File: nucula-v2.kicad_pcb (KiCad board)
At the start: 4 copper layers, 60 x 110 mm, 130 parts, among them J1 USB4105-GF-A-120, J2 JST-PH / 1S Li-ion, J3 KEYBOARD / USER FIT, J4 MAIN LINK / OPTIONAL, J5 MODULE LINK / OPTIONAL, Q1 IRLML6402, Q2 BSS138, Q3 IRLML6402, Q4 BSS138, Q5 BSS138, SW1 RESET, SW2 BOOT, U1 TP4054-42-SOT25R, U2 SY8089AAAC, U3 ESP32-C3-WROOM-02-N4, U4 USBLC6-2SC6, U5 TLV803EA30DBZR, U6 PN7160A1HN/C100E, U7 AP3012KTR-E1, U8 PCF8574T, U9 MCP1700T-3002E/TT, Y1 27.12MHz / CL 10pF

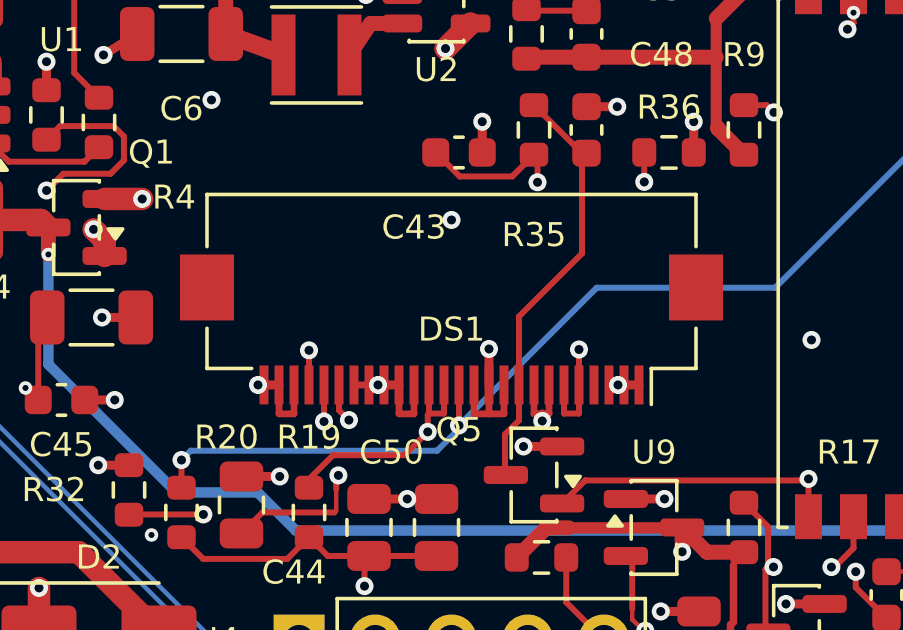
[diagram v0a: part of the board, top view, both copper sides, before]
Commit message: Correct OLED interface and routing for 24-pin display
Replace the 26-contact OLED symbol and socket with the verified CON24 pinout and Hirose FH12-24S connector. Preserve DS1 placement and all other board geometry while rerouting its local pad escapes. Update purchasing data, design exports and regression checks.

Validation: zero ERC/DRC errors, no unconnected items or schematic parity issues; 54 layout/regression checks pass; all 261 scoped simulation results unchanged. The two existing U3 silkscreen-edge warnings remain.
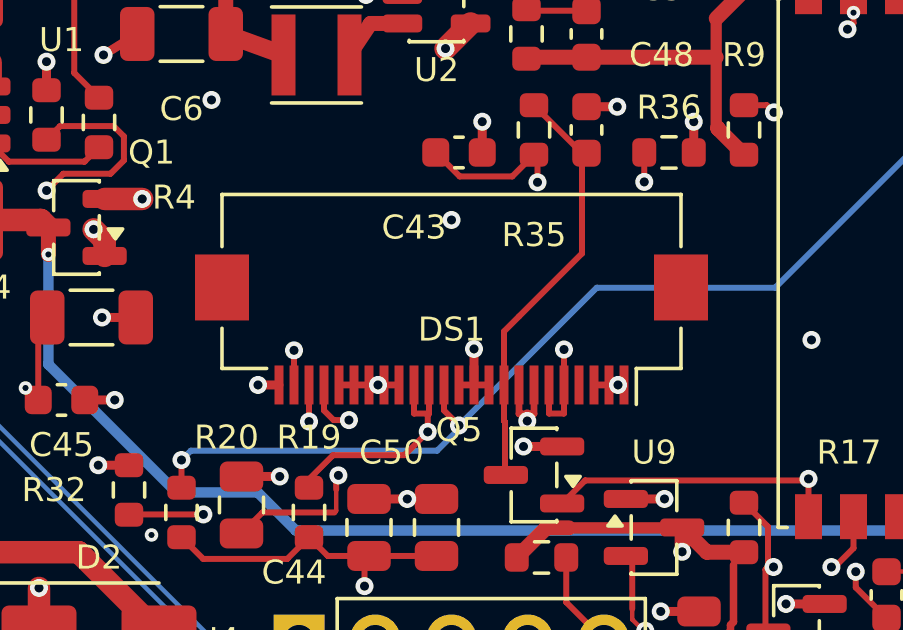
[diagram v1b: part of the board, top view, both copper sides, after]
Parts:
- DS1: value SSD1309 OLED / 26-pin -> SSD1309 OLED / 24-pin; footprint Connector_FFC-FPC:Hirose_FH12-26S-0.5SH_1x26-1MP_P0.50mm_Horizontal -> Connector_FFC-FPC:Hirose_FH12-24S-0.5SH_1x24-1MP_P0.50mm_Horizontal
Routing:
- net GND: track 235.3 -> 227.9 mm
- net /OLED / SSD1309 / 0x3C/OLED_IREF: track 10.0 -> 10.5 mm
- net /OLED / SSD1309 / 0x3C/OLED_12V5: track 61.6 -> 61.1 mm

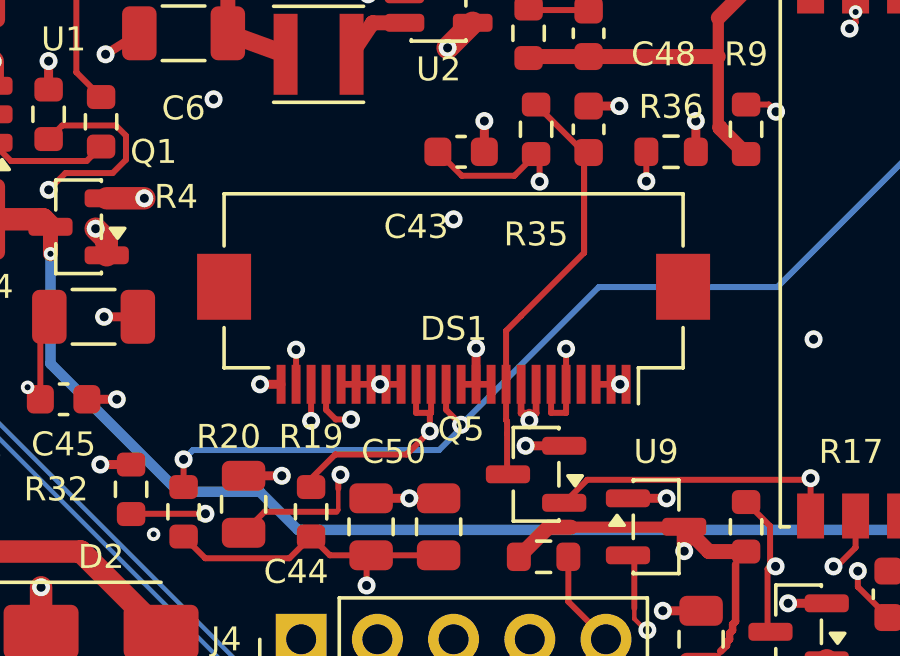
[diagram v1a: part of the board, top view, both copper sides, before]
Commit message: Use top-contact OLED connector and document manufacturing preparation
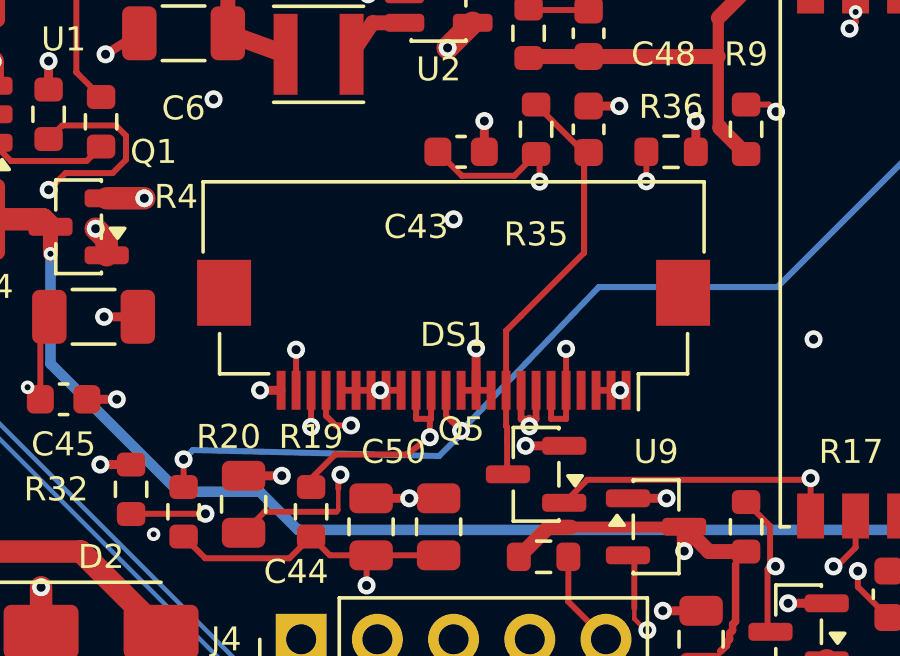
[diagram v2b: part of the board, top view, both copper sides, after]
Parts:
- DS1: footprint Connector_FFC-FPC:Hirose_FH12-24S-0.5SH_1x24-1MP_P0.50mm_Horizontal -> Nucula_Project:Hirose_FH12A-24S-0.5SH_1x24-1MP_P0.50mm_Horizontal
- moved DS1 0.20 mm to (80.0, 108.8)

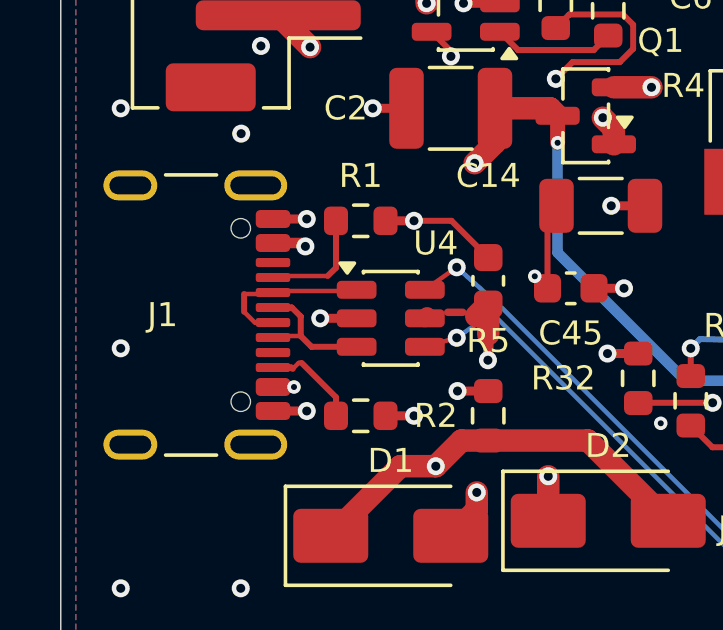
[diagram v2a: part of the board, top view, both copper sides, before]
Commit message: Fix USB connector clearance and prepare JLCPCB manufacturing release
Trim the two outer USB4105 ground lands by 0.04 mm at the locating-hole end, raising nominal NPTH clearance to 0.2333 mm. Use a project-local footprint and enforce JLCPCB's 0.20 mm minimum.

Regenerate Gerbers, drills, assembly files, drawings and source/hash archives. Refresh stock and ten-board purchasing quantities; add native and independent geometry validation. Preserve all placement, routing, holes and the confirmed OLED interface.
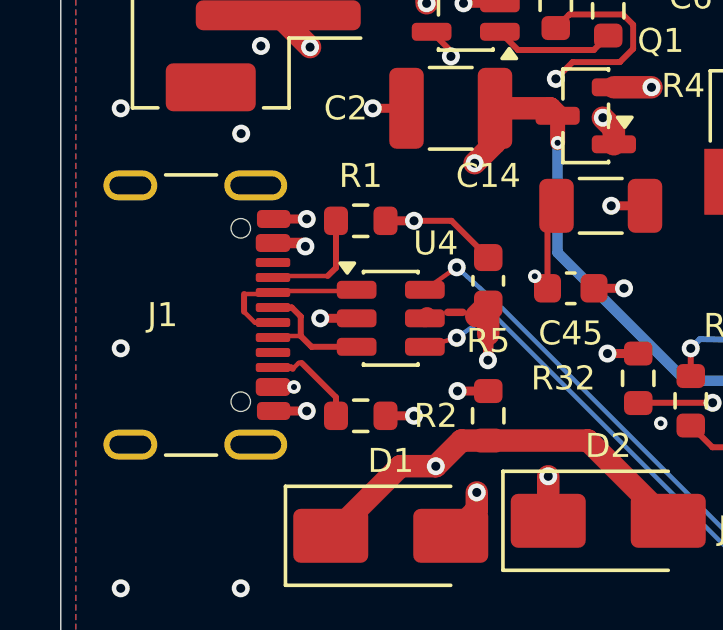
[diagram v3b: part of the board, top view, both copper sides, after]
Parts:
- J1: footprint Connector_USB:USB_C_Receptacle_GCT_USB4105-xx-A_16P_TopMnt_Horizontal -> Nucula_Project:USB_C_GCT_USB4105_16P_JLCPCB
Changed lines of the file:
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@@
 		)
 	)
-	(footprint "Connector_USB:USB_C_Receptacle_GCT_USB4105-xx-A_16P_TopMnt_Horizontal"
+	(footprint "Nucula_Project:USB_C_GCT_USB4105_16P_JLCPCB"
 		(locked yes)
 		(layer "F.Cu")
@@
 		)
 		(pad "A1" smd roundrect
-			(at -3.2 -3.68 270)
-			(size 0.6 1.15)
+			(at -3.2 -3.7 270)
+			(size 0.6 1.11)
 			(layers "F.Cu" "F.Mask" "F.Paste")
 			(roundrect_rratio 0.25)
@@
 		)
 		(pad "A12" smd roundrect
-			(at 3.2 -3.68 270)
-			(size 0.6 1.15)
+			(at 3.2 -3.7 270)
+			(size 0.6 1.11)
 			(layers "F.Cu" "F.Mask" "F.Paste")
 			(roundrect_rratio 0.25)
@@
 		)
 		(pad "B1" smd roundrect
-			(at 3.2 -3.68 270)
-			(size 0.6 1.15)
+			(at 3.2 -3.7 270)
+			(size 0.6 1.11)
 			(layers "F.Cu" "F.Mask" "F.Paste")
 			(roundrect_rratio 0.25)
@@
 		)
 		(pad "B12" smd roundrect
-			(at -3.2 -3.68 270)
-			(size 0.6 1.15)
-			(layers "F.Cu" "F.Mask" "F.Paste")
-			(roundrect_rratio 0.25)
+			(at -3.2 -3.7 270)
+			(size 0.6 1.11)
+			(layers "F.Cu" "F.Mask" "F.Paste")
+			(roundrect_rratio 0.25)
